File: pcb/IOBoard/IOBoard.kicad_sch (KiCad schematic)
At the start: 13 parts, among them J1 XT60PW-M, J2 TYPE-C-31-M-12, J4 DNP, J5 Right Angle 1x4, J6 FH41-40S-0.5SH_05_

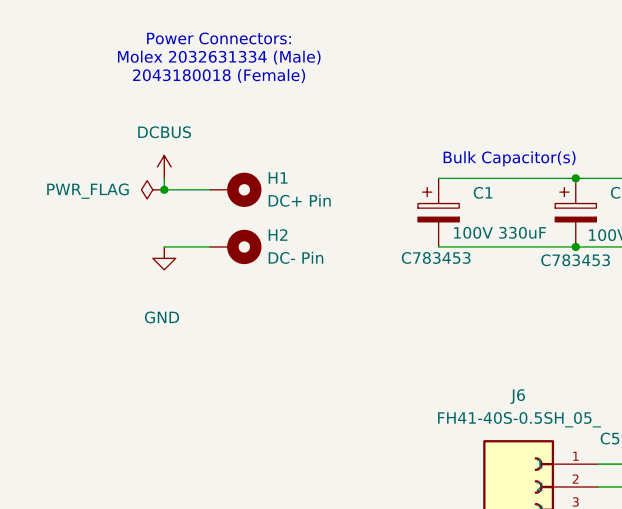
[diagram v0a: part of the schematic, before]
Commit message: Renamed folder names
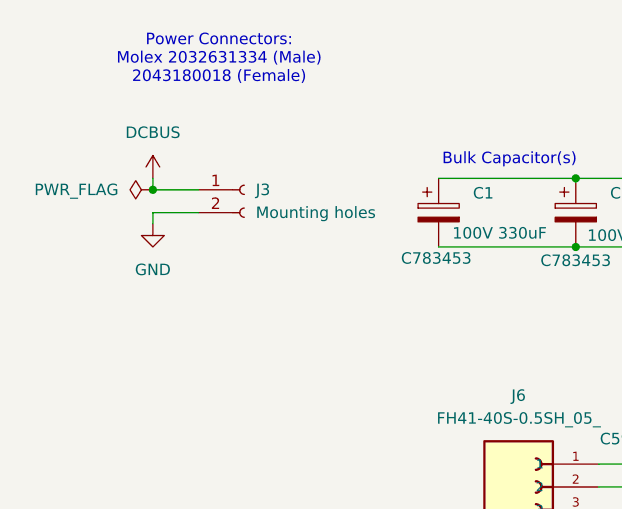
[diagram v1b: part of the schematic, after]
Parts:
- removed H1: DC+ Pin, symbol Mechanical:MountingHole_Pad
- removed H2: DC- Pin, symbol Mechanical:MountingHole_Pad
- added J3: Mounting holes, holes:Dual Post, symbol Connector:Conn_01x02_Socket
- C1, C2: footprint (none) -> Capacitor_THT:CP_Radial_D13.0mm_P5.00mm
- J1: footprint CONN_XT60PW-M_AMA -> footprints:CONN_XT60PW-M_AMA
- J4: footprint L8AL-1X1T-32A:BEL_L8AL-1X1T-32A -> RJ45:BEL_L8AL-1X1T-32A
- J5: footprint (none) -> Connector_PinHeader_2.54mm:PinHeader_1x04_P2.54mm_Horizontal
- J6: footprint FH41-40S-0.5SH_05_:HRS_FH41-40S-0.5SH_05_ -> FH41:HRS_FH41-40S-0.5SH_05_
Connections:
- net DCBUS: now also J3.1 (Pin_1)
- net GND: now also J3.2 (Pin_2)
